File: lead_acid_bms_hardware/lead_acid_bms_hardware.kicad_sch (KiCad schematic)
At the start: 75 parts, among them J1 debugging_connector, J2 battery_p, J3 battery_n, J4 bms_p, J5 bms_n, Q1 IRFZ44N, Q10 CJ2305, Q11 CJ2305, Q2 IRFZ44N, Q3 MMBT3904, Q4 CJ2305, Q5 MMBT3904, Q6 S9015, Q7 MMBT3904, Q8 MMBT3904, Q9 S9015, SW1 rst, U1 AMS1117-3.3, U2 TL974IDR, U3 ATmega8-16A, U4 NRF24L01_Breakout

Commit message: Added NTC for temperature measurements
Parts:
- gave numbers to parts that had none: 4
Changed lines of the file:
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@@
       (effects (font (size 1.27 1.27)) hide)
     )
-    (pin "1")
-    (pin "2")
-    (pin "3")
-    (pin "5")
-    (pin "6")
-    (pin "7")
     (pin "10")
     (pin "8")
     (pin "9")
-    (pin "12")
-    (pin "13")
-    (pin "14")
-    (pin "11")
-    (pin "4")
   )
   (symbol (lib_id "Device:R") (at 83.82 254 90) (unit 1)
@@
   (symbol (lib_id "Device:R") (at 68.58 144.78 0) (unit 1)
     (in_bom yes) (on_board yes) (fields_autoplaced)
-    (property "Reference" "R?" (id 0) (at 71.12 143.5099 0)
+    (property "Reference" "R42" (id 0) (at 71.12 143.5099 0)
       (effects (font (size 1.27 1.27)) (justify left))
     )
@@
       (effects (font (size 1.27 1.27)) hide)
     )
-    (pin "1")
-    (pin "2")
-    (pin "3")
-    (pin "5")
-    (pin "6")
-    (pin "7")
-    (pin "10")
-    (pin "8")
-    (pin "9")
     (pin "12")
     (pin "13")
     (pin "14")
-    (pin "11")
-    (pin "4")
   )
   (symbol (lib_id "Device:Opamp_Quad") (at 238.76 76.2 0) (unit 2)
@@
       (effects (font (size 1.27 1.27)) hide)
     )
-    (pin "1")
-    (pin "2")
-    (pin "3")
     (pin "5")
     (pin "6")
     (pin "7")
-    (pin "10")
-    (pin "8")
-    (pin "9")
-    (pin "12")
-    (pin "13")
-    (pin "14")
-    (pin "11")
-    (pin "4")
   )
   (symbol (lib_id "Device:R") (at 240.03 46.99 270) (unit 1)
@@
   (symbol (lib_id "Device:C") (at 307.34 88.9 0) (mirror x) (unit 1)
     (in_bom yes) (on_board yes) (fields_autoplaced)
-    (property "Reference" "C?" (id 0) (at 303.53 87.6299 0)
+    (property "Reference" "C7" (id 0) (at 303.53 87.6299 0)
       (effects (font (size 1.27 1.27)) (justify right))
     )
@@
     (pin "2")
     (pin "3")
-    (pin "5")
-    (pin "6")
-    (pin "7")
-    (pin "10")
-    (pin "8")
-    (pin "9")
-    (pin "12")
-    (pin "13")
-    (pin "14")
-    (pin "11")
-    (pin "4")
   )
   (symbol (lib_id "Device:R") (at 224.79 109.22 90) (unit 1)
@@
   (symbol (lib_id "Device:Thermistor_NTC") (at 68.58 134.62 0) (unit 1)
     (in_bom yes) (on_board yes) (fields_autoplaced)
-    (property "Reference" "TH?" (id 0) (at 71.12 133.6674 0)
+    (property "Reference" "TH1" (id 0) (at 71.12 133.6674 0)
       (effects (font (size 1.27 1.27)) (justify left))
     )
@@
   (symbol (lib_id "Device:C") (at 321.31 88.9 0) (mirror x) (unit 1)
     (in_bom yes) (on_board yes) (fields_autoplaced)
-    (property "Reference" "C?" (id 0) (at 317.5 87.6299 0)
+    (property "Reference" "C8" (id 0) (at 317.5 87.6299 0)
       (effects (font (size 1.27 1.27)) (justify right))
     )
@@
   (symbol (lib_id "power:+3V3") (at 321.31 83.82 0) (unit 1)
     (in_bom yes) (on_board yes) (fields_autoplaced)
-    (property "Reference" "#PWR?" (id 0) (at 321.31 87.63 0)
+    (property "Reference" "#PWR0101" (id 0) (at 321.31 87.63 0)
       (effects (font (size 1.27 1.27)) hide)
     )
@@
       (effects (font (size 1.27 1.27)) hide)
     )
-    (pin "1")
-    (pin "2")
-    (pin "3")
-    (pin "5")
-    (pin "6")
-    (pin "7")
-    (pin "10")
-    (pin "8")
-    (pin "9")
-    (pin "12")
-    (pin "13")
-    (pin "14")
     (pin "11")
     (pin "4")
@@
   (symbol (lib_id "power:+3V3") (at 307.34 83.82 0) (unit 1)
     (in_bom yes) (on_board yes) (fields_autoplaced)
-    (property "Reference" "#PWR?" (id 0) (at 307.34 87.63 0)
+    (property "Reference" "#PWR0102" (id 0) (at 307.34 87.63 0)
       (effects (font (size 1.27 1.27)) hide)
     )
@@
     )
     (path "/a1d343ea-86ac-4e4a-b7ae-8d69570ab35d"
-      (reference "#PWR?") (unit 1) (value "+3V3") (footprint "")
+      (reference "#PWR0101") (unit 1) (value "+3V3") (footprint "")
     )
     (path "/f246fcc1-a435-4d11-a9c9-4a10544d5aa4"
-      (reference "#PWR?") (unit 1) (value "+3V3") (footprint "")
+      (reference "#PWR0102") (unit 1) (value "+3V3") (footprint "")
     )
     (path "/d088b643-6c29-43a0-84cb-bf5ec597bdb7"
@@
     )
     (path "/50c384f2-a8bb-45aa-afa1-f9a173349f84"
-      (reference "C?") (unit 1) (value "100nF") (footprint "Capacitor_SMD:C_0805_2012Metric")
+      (reference "C7") (unit 1) (value "100nF") (footprint "Capacitor_SMD:C_0805_2012Metric")
     )
     (path "/98583760-3aba-4b9f-b2e4-f2ed4544d1d4"
-      (reference "C?") (unit 1) (value "100nF") (footprint "Capacitor_SMD:C_0805_2012Metric")
+      (reference "C8") (unit 1) (value "100nF") (footprint "Capacitor_SMD:C_0805_2012Metric")
     )
     (path "/e934b282-db34-41ce-a3e5-90776ddf82de"
@@
     )
     (path "/24c7f498-51b5-444c-871b-8f18707a49d9"
-      (reference "R?") (unit 1) (value "10k") (footprint "Resistor_SMD:R_0805_2012Metric")
+      (reference "R42") (unit 1) (value "10k") (footprint "Resistor_SMD:R_0805_2012Metric")
     )
     (path "/61072f30-e813-41d9-8eca-ec049ea9a89c"
@@
     )
     (path "/85874c82-f3c1-439f-89c7-e9f852f30c23"
-      (reference "TH?") (unit 1) (value "3977K") (footprint "Connector_PinSocket_2.54mm:PinSocket_1x02_P2.54mm_Vertical")
+      (reference "TH1") (unit 1) (value "3977K") (footprint "Connector_PinSocket_2.54mm:PinSocket_1x02_P2.54mm_Vertical")
     )
     (path "/4ae472c4-7cc5-4002-9947-6534bffcc617"

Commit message: Routing...
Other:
- note added: "Switch for 3V3 circuitry"
- note removed: "Switch for current measurement"
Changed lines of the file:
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@@
     (effects (font (size 1.27 1.27)) (justify left bottom))
   )
-  (text "Switch for current measurement" (at 113.03 58.42 0)
+  (text "Switch for 3V3 circuitry" (at 113.03 58.42 0)
     (effects (font (size 1.27 1.27)) (justify left bottom))
   )
@@
       (effects (font (size 1.27 1.27)) hide)
     )
+    (pin "1")
+    (pin "2")
+    (pin "3")
+    (pin "5")
+    (pin "6")
+    (pin "7")
     (pin "10")
     (pin "8")
     (pin "9")
+    (pin "12")
+    (pin "13")
+    (pin "14")
+    (pin "11")
+    (pin "4")
   )
   (symbol (lib_id "Device:R") (at 83.82 254 90) (unit 1)
@@
       (effects (font (size 1.27 1.27)) hide)
     )
+    (pin "1")
+    (pin "2")
+    (pin "3")
+    (pin "5")
+    (pin "6")
+    (pin "7")
+    (pin "10")
+    (pin "8")
+    (pin "9")
     (pin "12")
     (pin "13")
     (pin "14")
+    (pin "11")
+    (pin "4")
   )
   (symbol (lib_id "Device:Opamp_Quad") (at 238.76 76.2 0) (unit 2)
@@
       (effects (font (size 1.27 1.27)) hide)
     )
+    (pin "1")
+    (pin "2")
+    (pin "3")
     (pin "5")
     (pin "6")
     (pin "7")
+    (pin "10")
+    (pin "8")
+    (pin "9")
+    (pin "12")
+    (pin "13")
+    (pin "14")
+    (pin "11")
+    (pin "4")
   )
   (symbol (lib_id "Device:R") (at 240.03 46.99 270) (unit 1)
@@
     (pin "2")
     (pin "3")
+    (pin "5")
+    (pin "6")
+    (pin "7")
+    (pin "10")
+    (pin "8")
+    (pin "9")
+    (pin "12")
+    (pin "13")
+    (pin "14")
+    (pin "11")
+    (pin "4")
   )
   (symbol (lib_id "Device:R") (at 224.79 109.22 90) (unit 1)
@@
       (effects (font (size 1.27 1.27)) hide)
     )
+    (pin "1")
+    (pin "2")
+    (pin "3")
+    (pin "5")
+    (pin "6")
+    (pin "7")
+    (pin "10")
+    (pin "8")
+    (pin "9")
+    (pin "12")
+    (pin "13")
+    (pin "14")
     (pin "11")
     (pin "4")

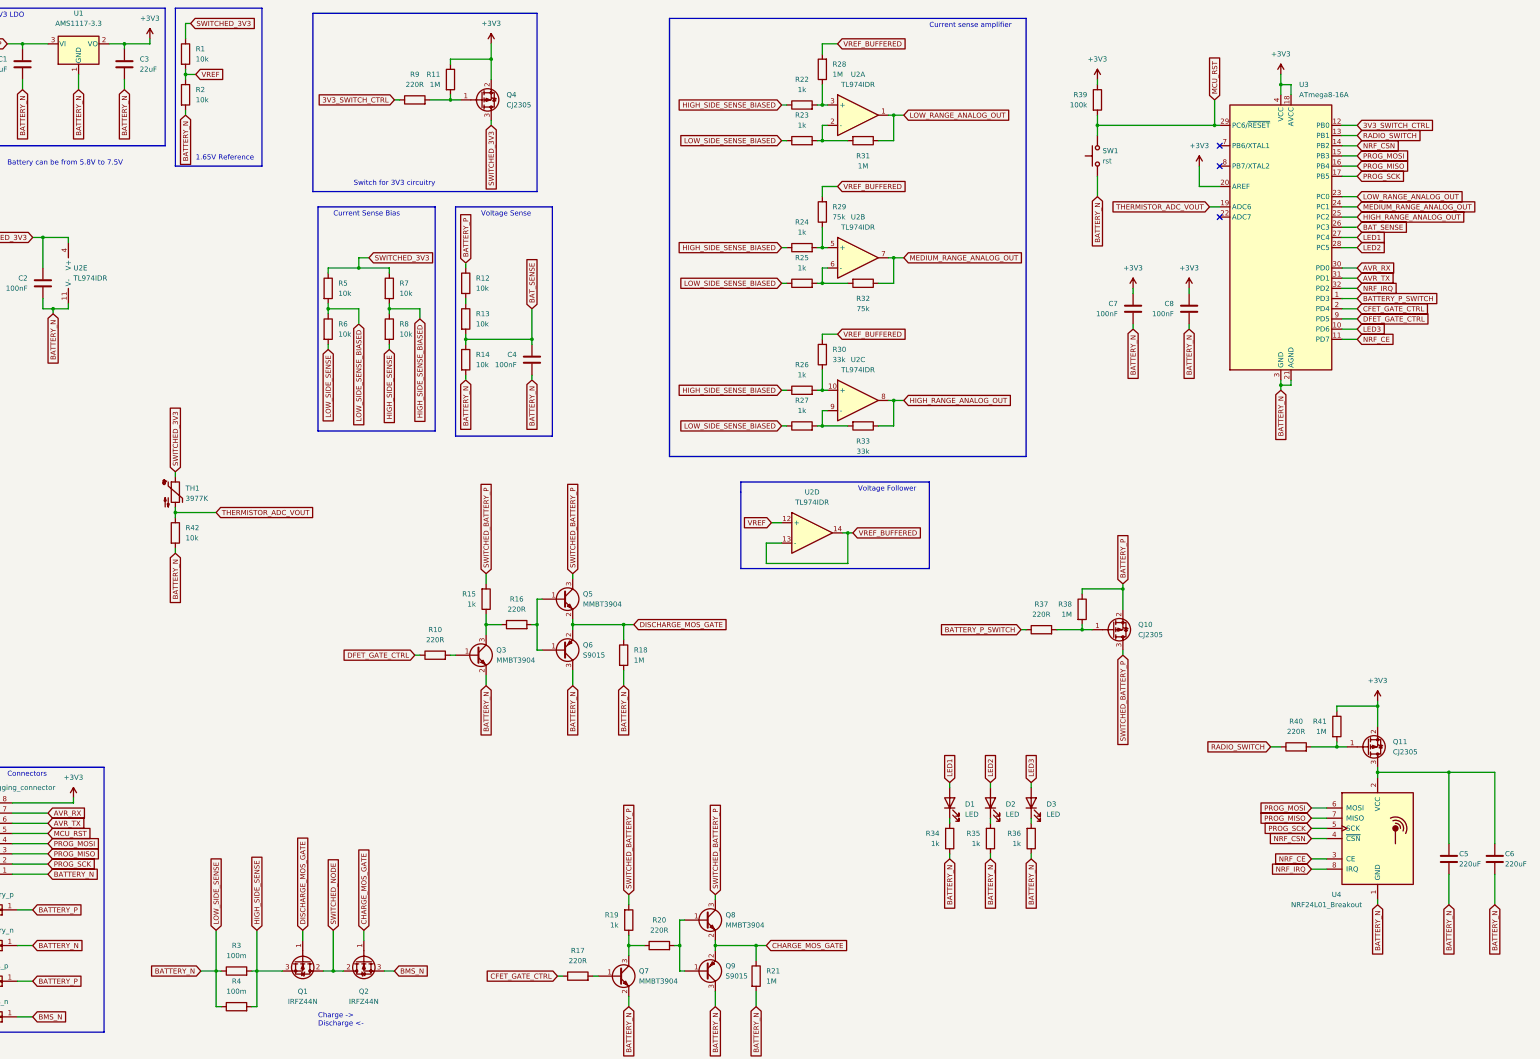
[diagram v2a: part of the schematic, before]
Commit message: Almost done with PCB placement/routing. Need to find lower power amplifier (TL974IDR is not good enough)
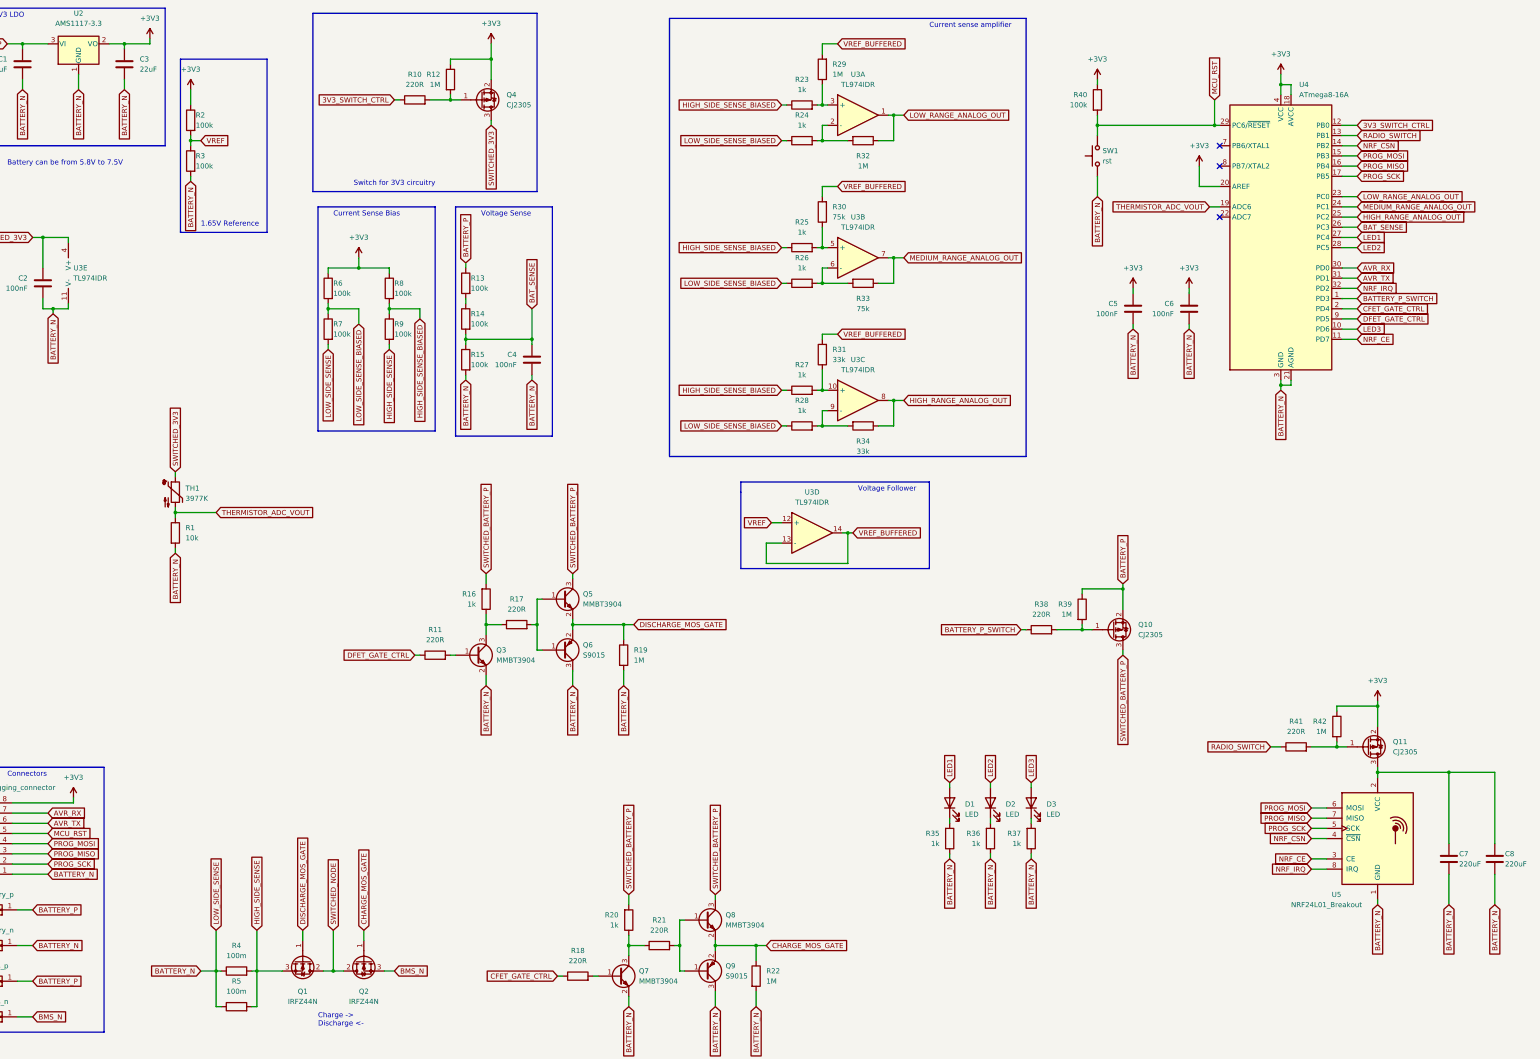
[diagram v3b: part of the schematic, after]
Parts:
- removed R1, R12, R5: 10k, Resistor_SMD:R_0805_2012Metric, symbol Device:R
- added R15, R3, R9: 100k, Resistor_SMD:R_0805_2012Metric, symbol Device:R
- R13, R14, R2, R6, R7, R8: value 10k -> 100k
- renumbered C7 to C5, C8 to C6, C5 to C7, C6 to C8, R42 to R1, R9 to R10, R10 to R11, R11 to R12, R15 to R16, R16 to R17, R17 to R18, R18 to R19, R19 to R20, R20 to R21, R21 to R22, R22 to R23, R23 to R24, R24 to R25, R25 to R26, R26 to R27, R27 to R28, R28 to R29, R29 to R30, R30 to R31, R31 to R32, R32 to R33, R33 to R34, R34 to R35, R35 to R36, R36 to R37, R37 to R38, R38 to R39, R3 to R4, R39 to R40, R40 to R41, R41 to R42, R4 to R5, U1 to U2, U2 to U3, U3 to U4, U4 to U5
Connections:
- net +3V3: now also R2.1, R6.1, R8.1
- net BATTERY_N: now also R7.2, R15.2, R3.2; no longer R14.2, R2.2, R6.2
- net BATTERY_P: now also R13.1
- net BAT_SENSE: now also R14.2, R15.1; no longer R13.2, R14.1
- net HIGH_SIDE_SENSE: now also R9.2; no longer R8.2
- net HIGH_SIDE_SENSE_BIASED: now also R8.2, R9.1; no longer R7.2, R8.1
- net LOW_SIDE_SENSE_BIASED: now also R6.2, R7.1; no longer R6.1
- net SWITCHED_3V3: no longer R7.1
- net VREF: now also R2.2, R3.1; no longer R2.1
- new net: R13.2, R14.1
